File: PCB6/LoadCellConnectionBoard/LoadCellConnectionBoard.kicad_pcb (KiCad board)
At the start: 2 copper layers, 86 x 58.5 mm, 18 parts, among them P1 CONN_02X02, P10 CONN_01X15, P2 CONN_02X02, P3 CONN_02X02, P4 CONN_02X02, P5 CONN_02X02, P6 CONN_02X02, P7 CONN_02X02, P8 CONN_02X02, P9 CONN_01X15

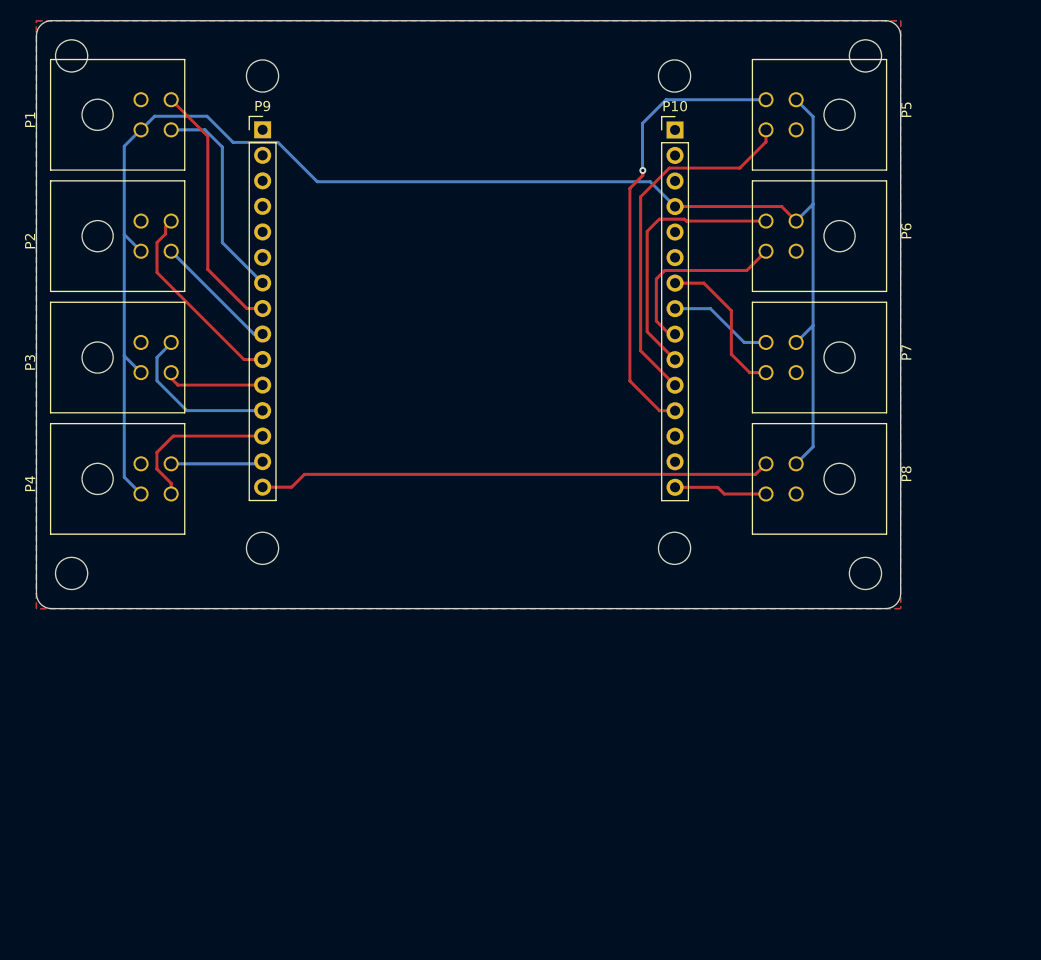
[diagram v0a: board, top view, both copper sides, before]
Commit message: Placa driver casi enrutada, step y medidas exportadas
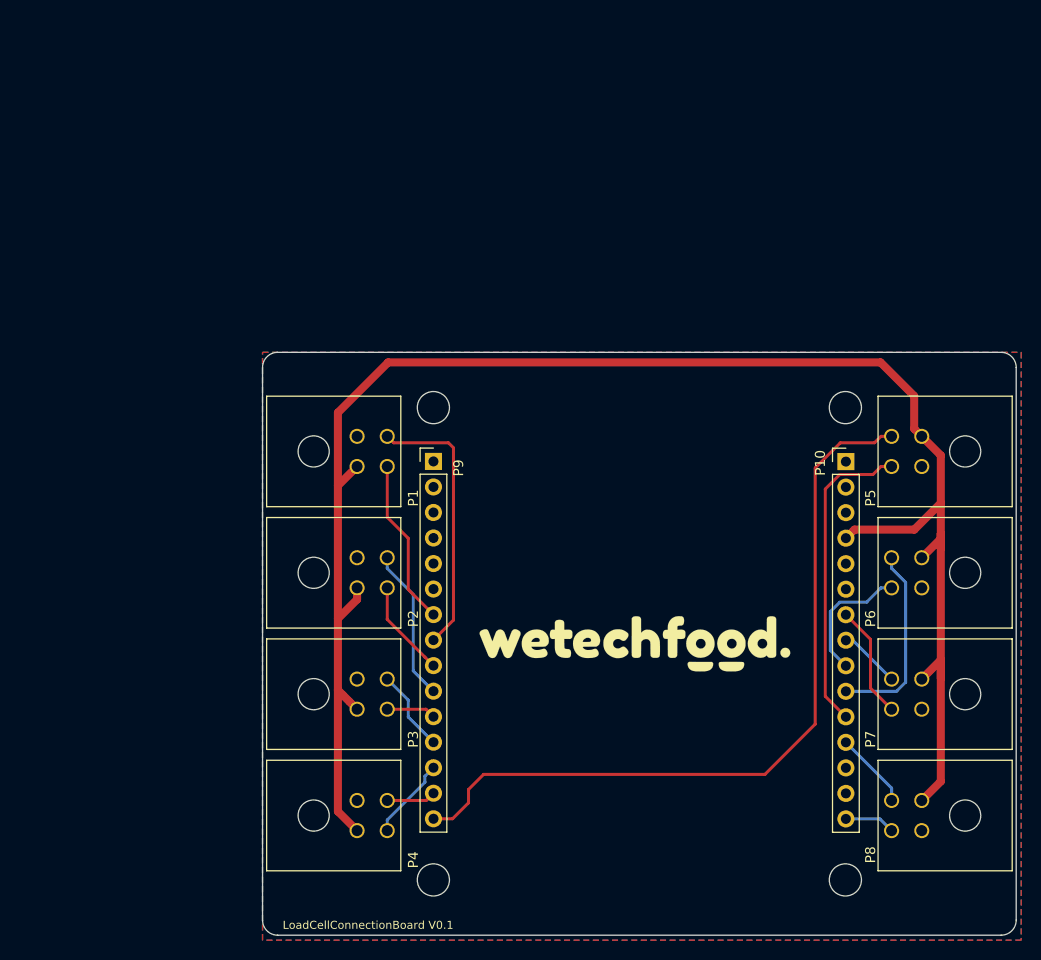
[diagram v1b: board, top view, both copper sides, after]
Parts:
- removed the REF** at (90.5, 42.5)
- removed the REF** at (169.5, 42.5)
- removed the REF** at (169.5, 94.0)
- removed the REF** at (90.5, 94.0)
- removed the REF** at (150.5, 44.5)
- removed the REF** at (109.5, 44.5)
- removed the REF** at (109.5, 91.5)
- removed the REF** at (150.5, 91.5)
- added G***: LOGO, logos_frizzy:logoWTF_small, F.Cu at (146.5, 101.0)
- added REF**: MountingHole_3.2mm_M3, Mounting_Holes:MountingHole_3.2mm_M3, F.Cu at (126.5, 124.5)
- added REF**: MountingHole_3.2mm_M3, Mounting_Holes:MountingHole_3.2mm_M3, F.Cu at (126.5, 77.5)
- added REF**: MountingHole_3.2mm_M3, Mounting_Holes:MountingHole_3.2mm_M3, F.Cu at (167.5, 77.5)
- added REF**: MountingHole_3.2mm_M3, Mounting_Holes:MountingHole_3.2mm_M3, F.Cu at (167.5, 124.5)
- moved P1 39.8 mm to (118.9, 83.4)
- moved P2 39.8 mm to (118.9, 95.4)
- moved P3 39.8 mm to (118.9, 107.5)
- moved P4 39.8 mm to (118.9, 119.6)
- moved P10 37.1 mm to (167.6, 82.9)
- moved P9 37.1 mm to (126.5, 82.9)
- moved P5 35.8 mm to (175.1, 80.4)
- moved P6 35.8 mm to (175.1, 92.4)
- moved P7 35.8 mm to (175.1, 104.5)
- moved P8 35.8 mm to (175.1, 116.6)
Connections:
- P10 pad 12: DT5 -> DT8
- P9 pad 15: DT8 -> DT5
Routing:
- net DT8: track 51.1 -> 7.67 mm
- net DT5: track 45.2 -> 77.1 mm, vias 1 -> 0
- net VCC: track 154.8 -> 174.8 mm
- net SCK3: track 16.1 -> 8.19 mm
- net DT4: track 15.9 -> 8.16 mm
- net DT6: track 26.3 -> 19.3 mm
- net SCK6: track 18.7 -> 13.1 mm
- net SCK5: track 36.1 -> 31.0 mm
- net DT3: track 9.95 -> 4.91 mm
- net SCK2: track 19.8 -> 15.2 mm
- net DT1: track 21.0 -> 16.6 mm
- net SCK8: track 9.32 -> 5.03 mm
- net DT7: track 10.4 -> 6.15 mm
- net SCK4: track 9.19 -> 4.90 mm
- net SCK7: track 15.3 -> 11.3 mm
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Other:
- board size 86 x 58.5 mm -> 75 x 58 mm
- board text added: "LoadCellConnectionBoard V0.1"
